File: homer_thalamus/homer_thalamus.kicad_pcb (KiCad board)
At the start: 4 copper layers, 95 x 56 mm, 5 parts, among them J1 GPIO

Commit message: update pcb layout
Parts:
- added A1: RaspberryPi_Pico, Module:RaspberryPi_Pico_Common_Unspecified, F.Cu at (139.2, 72.2)
- added ACC1: GY-521, GY-521:GY-521, F.Cu at (110.3, 61.4)
- added C1: 100n, Capacitor_THT:C_Disc_D4.7mm_W2.5mm_P5.00mm, F.Cu at (178.2, 110.6)
- added D1: LED_RKGB, LED_THT:LED_D5.0mm-4_RGB_Wide_Pins, F.Cu at (174.0, 118.8)
- added J2: MotDrv_Pow_Conn, Connector_JST:JST_XH_B2B-XH-AM_1x02_P2.50mm_Vertical, F.Cu at (77.4, 104.8)
- added J3: Right_Motor_Conn, Connector_PinHeader_2.54mm:PinHeader_1x06_P2.54mm_Vertical, F.Cu at (76.8, 47.0)
- added J4: Left_Motor_Conn, Connector_PinHeader_2.54mm:PinHeader_1x06_P2.54mm_Vertical, F.Cu at (77.6, 97.9)
- added J5: Spare_GP_Conn, Connector_PinHeader_2.54mm:PinHeader_1x10_P2.54mm_Vertical, F.Cu at (140.2, 57.6)
- added J6: VBUS_Conn, Connector_PinHeader_2.54mm:PinHeader_2x02_P2.54mm_Vertical, F.Cu at (177.1, 91.1)
- added R1: 1K, Resistor_THT:R_Axial_DIN0207_L6.3mm_D2.5mm_P7.62mm_Horizontal, F.Cu at (201.6, 90.4)
- added R2: 220R, Resistor_THT:R_Axial_DIN0207_L6.3mm_D2.5mm_P7.62mm_Horizontal, F.Cu at (197.6, 90.4)
- added R3: 220R, Resistor_THT:R_Axial_DIN0207_L6.3mm_D2.5mm_P7.62mm_Horizontal, F.Cu at (193.5, 90.4)
- added R4: 220R, Resistor_THT:R_Axial_DIN0207_L6.3mm_D2.5mm_P7.62mm_Horizontal, F.Cu at (189.5, 90.4)
- added R5: 2K, Resistor_THT:R_Axial_DIN0207_L6.3mm_D2.5mm_P7.62mm_Horizontal, F.Cu at (185.4, 90.4)
- added R6: 1K, Resistor_THT:R_Axial_DIN0207_L6.3mm_D2.5mm_P7.62mm_Horizontal, F.Cu at (181.4, 90.4)
- added SW1: SW_PULLDOWN, Button_Switch_THT:SW_PUSH_6mm, F.Cu at (184.3, 119.2)
- added U1: DRV8874_CARRIER_RIGHT, DRV8874_Carrier:DRV8874_Carrier, F.Cu at (74.6, 65.6)
- added U2: DRV8874_CARRIER_LEFT, DRV8874_Carrier:DRV8874_Carrier, F.Cu at (92.0, 79.8)
- added U3: HC-SR04, HC-SR04:XCVR_HC-SR04, F.Cu at (72.5, 71.9)

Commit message: update pcb layout
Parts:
- moved U2 19.0 mm to (110.8, 76.7)
- moved ACC1 18.9 mm to (91.4, 59.6)
- moved U1 18.1 mm to (92.5, 68.4)
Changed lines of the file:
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@@
 	(footprint "DRV8874_Carrier:DRV8874_Carrier"
 		(layer "F.Cu")
-		(at 74.6373 65.5573 90)
+		(at 92.54 68.44 90)
 		(property "Reference" "U1"
 			(at 13.208 18.796 90)
@@
 			(polygon
 				(pts
-					(xy 74.6427 65.5427) (xy 74.6427 50.3427) (xy 92.4427 50.3427) (xy 92.4427 65.5427)
+					(xy 92.5454 68.4254) (xy 92.5454 53.2254) (xy 110.3454 53.2254) (xy 110.3454 68.4254)
 				)
 			)
@@
 			(polygon
 				(pts
-					(xy 74.6427 65.5427) (xy 74.6427 50.3427) (xy 92.4427 50.3427) (xy 92.4427 65.5427)
+					(xy 92.5454 68.4254) (xy 92.5454 53.2254) (xy 110.3454 53.2254) (xy 110.3454 68.4254)
 				)
 			)
@@
 	(footprint "GY-521:GY-521"
 		(layer "F.Cu")
-		(at 110.2616 61.4334 180)
+		(at 91.4416 59.5934 180)
 		(property "Reference" "ACC1"
 			(at 3.167 -22.8854 0)
@@
 	(footprint "DRV8874_Carrier:DRV8874_Carrier"
 		(layer "F.Cu")
-		(at 92.0027 79.7727 -90)
+		(at 110.78 76.74 -90)
 		(property "Reference" "U2"
 			(at 13.208 18.796 270)
@@
 			(polygon
 				(pts
-					(xy 91.9973 79.7873) (xy 91.9973 94.9873) (xy 74.1973 94.9873) (xy 74.1973 79.7873)
+					(xy 110.7746 76.7546) (xy 110.7746 91.9546) (xy 92.9746 91.9546) (xy 92.9746 76.7546)
 				)
 			)
@@
 			(polygon
 				(pts
-					(xy 91.9973 79.7873) (xy 91.9973 94.9873) (xy 74.1973 94.9873) (xy 74.1973 79.7873)
-				)
-			)
+					(xy 110.7746 76.7546) (xy 110.7746 91.9546) (xy 92.9746 91.9546) (xy 92.9746 76.7546)
+				)
+			)

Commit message: update layout
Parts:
- moved R6 103.9 mm to (78.9, 73.2), turned to 0 degrees
- moved R5 101.0 mm to (86.5, 70.1), turned to 180 degrees
- moved R1 89.4 mm to (112.3, 87.6), turned to 0 degrees
- moved SW1 76.9 mm to (112.7, 91.5), turned to 0 degrees
- moved C1 70.6 mm to (130.3, 58.8), turned to 0 degrees
- moved R2 65.1 mm to (132.8, 96.4), turned to 0 degrees
- moved R3 60.8 mm to (132.8, 93.3), turned to 0 degrees
- moved R4 56.7 mm to (132.8, 90.2), turned to 0 degrees
- moved D1 49.2 mm to (130.2, 96.4), turned to 180 degrees
- moved ACC1 19.7 mm to (111.0, 61.9)
- moved U1 18.1 mm to (74.7, 65.3)
- moved U2 17.1 mm to (94.0, 80.1)
- moved J6 15.2 mm to (162.0, 89.9), turned to 180 degrees
- moved J4 6.31 mm to (83.9, 97.6)
- moved U3 2.53 mm to (75.0, 72.0)
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
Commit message: update pcb layout
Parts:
- added ?: , , F.Cu at (79.3, 80.6)
- added ?: , , F.Cu at (79.3, 63.8)
- moved R5 44.5 mm to (124.1, 94.0)
- moved R6 41.4 mm to (116.4, 90.8)
- moved U1 34.8 mm to (109.2, 69.5), turned to 180 degrees
- moved J2 20.7 mm to (96.6, 97.0), turned to 180 degrees
- moved U2 18.9 mm to (109.2, 91.3), turned to 180 degrees
- moved ACC1 18.0 mm to (93.0, 61.8)
- moved R1 15.1 mm to (124.1, 97.2), turned to 180 degrees
- moved SW1 14.5 mm to (127.2, 92.6)
- moved R2 11.4 mm to (143.6, 92.8), turned to 90 degrees
- moved D1 9.88 mm to (134.0, 87.3)
- moved J4 9.48 mm to (74.5, 97.9)
- moved R3 7.64 mm to (140.4, 92.8), turned to 90 degrees
- moved R4 5.13 mm to (137.2, 92.8), turned to 90 degrees
- moved J6 4.30 mm to (163.1, 85.8), turned to -90 degrees
- moved J5 1.40 mm to (140.3, 56.3)
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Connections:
- J4 pad 5: /ENCA_L -> /ENCB_L
- J4 pad 6: /ENCB_L -> /ENCA_L

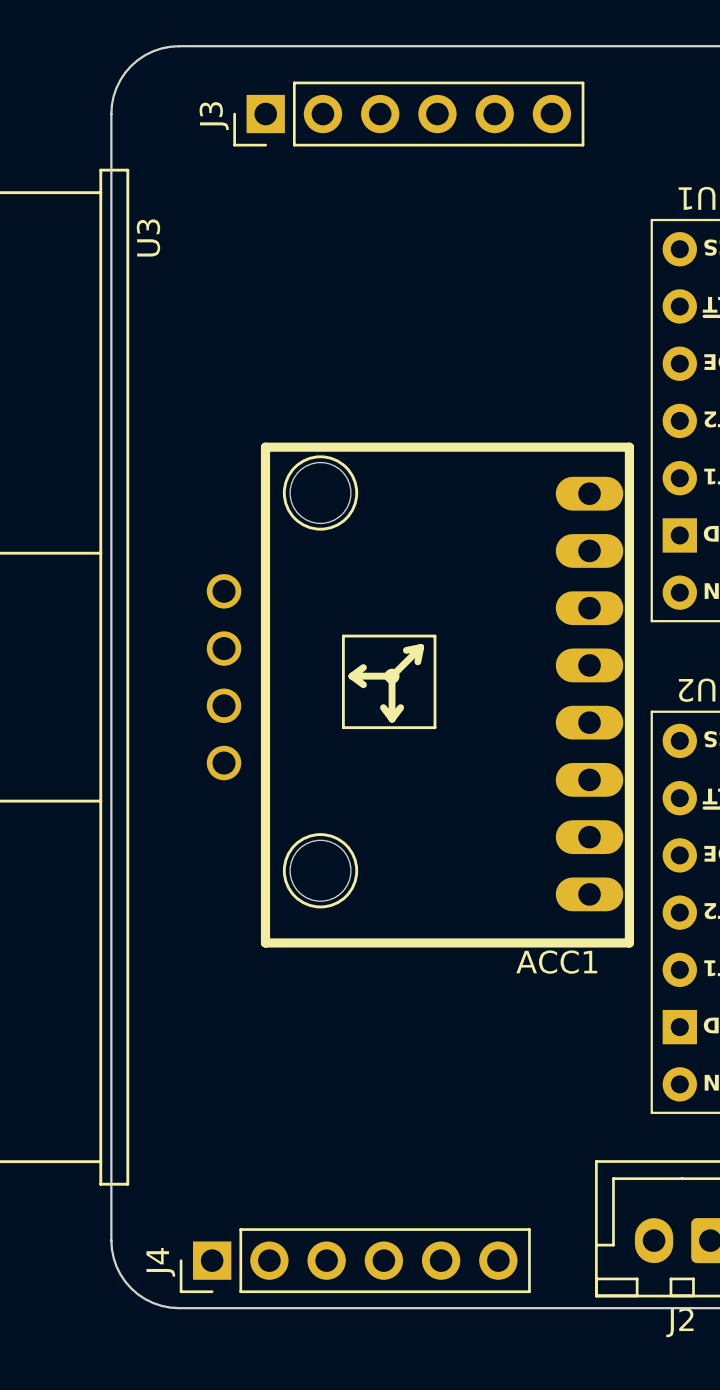
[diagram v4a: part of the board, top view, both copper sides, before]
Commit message: update motor connector position
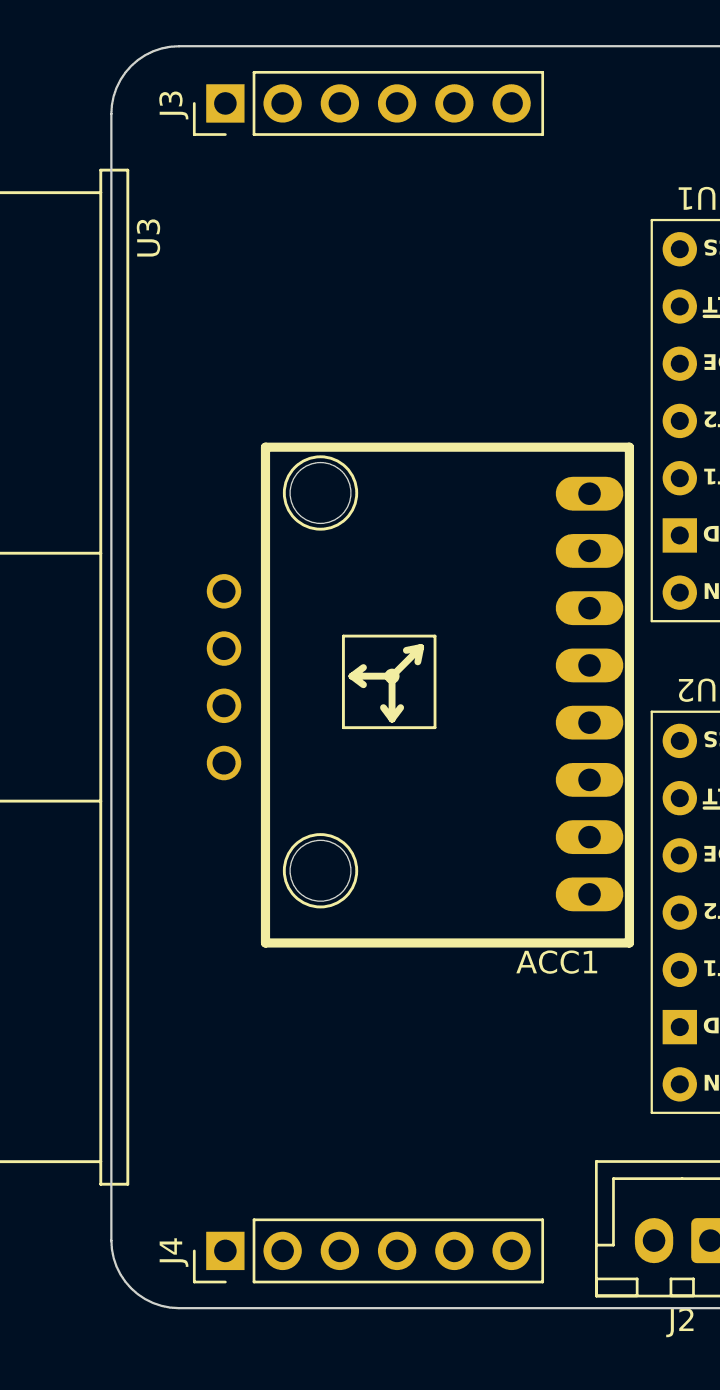
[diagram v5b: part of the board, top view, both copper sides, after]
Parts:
- moved J3 1.85 mm to (75.1, 46.5)
- moved J4 0.73 mm to (75.1, 97.5)
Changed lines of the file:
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@@
 	(footprint "Connector_PinHeader_2.54mm:PinHeader_1x06_P2.54mm_Vertical"
 		(layer "F.Cu")
-		(at 74.473 97.8918 90)
+		(at 75.06 97.46 90)
 		(descr "Through hole straight pin header, 1x06, 2.54mm pitch, single row")
 		(tags "Through hole pin header THT 1x06 2.54mm single row")
@@
 	)
 	(footprint "Connector_PinHeader_2.54mm:PinHeader_1x06_P2.54mm_Vertical"
+		(locked yes)
 		(layer "F.Cu")
-		(at 76.85 47.01 90)
+		(at 75.06 46.54 90)
 		(descr "Through hole straight pin header, 1x06, 2.54mm pitch, single row")
 		(tags "Through hole pin header THT 1x06 2.54mm single row")

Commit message: update pcb layout
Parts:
- moved J5 0.82 mm to (140.3, 55.5)
- moved U1 0.45 mm to (109.6, 69.5)
- moved J2 0.41 mm to (96.2, 96.9)
- moved C1 0.12 mm to (130.1, 58.7)
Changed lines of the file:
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@@
 	(footprint "Connector_JST:JST_XH_B2B-XH-AM_1x02_P2.50mm_Vertical"
 		(layer "F.Cu")
-		(at 96.5818 97.0028 180)
+		(at 96.1754 96.9266 180)
 		(descr "JST XH series connector, B2B-XH-AM, with boss (http://www.jst-mfg.com/product/pdf/eng/eXH.pdf), generated with kicad-footprint-generator")
 		(tags "connector JST XH vertical boss")
 		(property "Reference" "J2"
-			(at 1.25 -3.55 0)
+			(at 6.528 4.032 0)
 			(layer "F.SilkS")
 			(effects
@@
 	(footprint "DRV8874_Carrier:DRV8874_Carrier"
 		(layer "F.Cu")
-		(at 109.1948 69.52 180)
+		(at 109.64 69.46 180)
 		(property "Reference" "U1"
 			(at 13.208 18.796 180)
@@
 			(polygon
 				(pts
-					(xy 109.1802 69.5146) (xy 93.9802 69.5146) (xy 93.9802 51.7146) (xy 109.1802 51.7146)
+					(xy 109.6254 69.4546) (xy 94.4254 69.4546) (xy 94.4254 51.6546) (xy 109.6254 51.6546)
 				)
 			)
@@
 			(polygon
 				(pts
-					(xy 109.1802 69.5146) (xy 93.9802 69.5146) (xy 93.9802 51.7146) (xy 109.1802 51.7146)
+					(xy 109.6254 69.4546) (xy 94.4254 69.4546) (xy 94.4254 51.6546) (xy 109.6254 51.6546)
 				)
 			)
@@
 	(footprint "Capacitor_THT:C_Disc_D4.7mm_W2.5mm_P5.00mm"
 		(layer "F.Cu")
-		(at 130.052 58.598)
+		(at 130.11 58.6996)
 		(descr "C, Disc series, Radial, pin pitch=5.00mm, diameter*width=4.7*2.5mm^2, Capacitor, http://www.vishay.com/docs/45233/krseries.pdf")
 		(tags "C Disc series Radial pin pitch 5.00mm diameter 4.7mm width 2.5mm Capacitor")
@@
 		)
 		(property "Value" "100n"
-			(at 2.5 2.5 0)
-			(layer "F.Fab")
+			(at 2.5108 0.0346 0)
+			(layer "F.SilkS")
 			(effects
 				(font
@@
 	(footprint "Connector_PinHeader_2.54mm:PinHeader_1x10_P2.54mm_Vertical"
 		(layer "F.Cu")
-		(at 140.259 56.312 90)
+		(at 140.27 55.49 90)
 		(descr "Through hole straight pin header, 1x10, 2.54mm pitch, single row")
 		(tags "Through hole pin header THT 1x10 2.54mm single row")
@@
 		)
 	)
-	(group "MDs"
-		(members "6253dd3f-a163-4ecf-acd9-35d704d81902" "75fd1a30-d812-4647-95b3-fe729d1a6444")
-	)
 	(group ""

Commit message: update pcb layout
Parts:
- moved U3 2.46 mm to (72.5, 72.0)
- moved ? 1.75 mm to (77.6, 81.1)
- moved ? 1.75 mm to (77.6, 64.3)
- moved ACC1 1.75 mm to (91.3, 62.3)
- moved U1 1.44 mm to (108.5, 70.4)
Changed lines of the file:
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@@
 		(locked yes)
 		(layer "F.Cu")
-		(at 75 72 -90)
+		(at 72.54 72 -90)
 		(property "Reference" "U3"
-			(at -19.48505 3.31671 90)
+			(at -19.6758 3.0576 90)
 			(layer "F.SilkS")
 			(effects
@@
 		)
 		(property "Value" "HC-SR04"
-			(at 23.8102 3.370695 90)
-			(layer "F.Fab")
+			(at -0.0162 1.6738 90)
+			(layer "F.SilkS")
 			(effects
 				(font
@@
 	(footprint ""
 		(layer "F.Cu")
-		(at 79.2814 80.5906)
+		(at 77.5972 81.077)
 		(property "Reference" ""
 			(at 0 0 0)
@@
 	(footprint "DRV8874_Carrier:DRV8874_Carrier"
 		(layer "F.Cu")
-		(at 109.64 69.46 180)
+		(at 108.52 70.36 180)
 		(property "Reference" "U1"
 			(at 13.208 18.796 180)
@@
 			(polygon
 				(pts
-					(xy 109.6254 69.4546) (xy 94.4254 69.4546) (xy 94.4254 51.6546) (xy 109.6254 51.6546)
+					(xy 108.5054 70.3546) (xy 93.3054 70.3546) (xy 93.3054 52.5546) (xy 108.5054 52.5546)
 				)
 			)
@@
 			(polygon
 				(pts
-					(xy 109.6254 69.4546) (xy 94.4254 69.4546) (xy 94.4254 51.6546) (xy 109.6254 51.6546)
+					(xy 108.5054 70.3546) (xy 93.3054 70.3546) (xy 93.3054 52.5546) (xy 108.5054 52.5546)
 				)
 			)
@@
 	(footprint "GY-521:GY-521"
 		(layer "F.Cu")
-		(at 92.9894 61.7946 180)
+		(at 91.3052 62.281 180)
 		(property "Reference" "ACC1"
 			(at 3.167 -22.8854 0)
@@
 	(footprint ""
 		(layer "F.Cu")
-		(at 79.2814 63.8266)
+		(at 77.5972 64.313)
 		(property "Reference" ""
 			(at 0 0 0)

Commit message: update pcb layout
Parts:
- removed ? (x2): , 
- J2: footprint Connector_JST:JST_XH_B2B-XH-AM_1x02_P2.50mm_Vertical -> Connector_JST:JST_XH_B2B-XH-A_1x02_P2.50mm_Vertical
- moved J2 18.4 mm to (77.8, 96.7)
- moved J4 7.92 mm to (83.0, 97.8)
- moved J3 7.92 mm to (83.0, 46.2)
- moved J5 1.65 mm to (140.3, 53.8)
- moved U1 1.12 mm to (109.6, 70.4)
- moved U2 0.46 mm to (109.6, 91.5)
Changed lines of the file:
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@@
 		(embedded_fonts no)
 	)
-	(footprint "Connector_JST:JST_XH_B2B-XH-AM_1x02_P2.50mm_Vertical"
+	(footprint "Connector_JST:JST_XH_B2B-XH-A_1x02_P2.50mm_Vertical"
 		(layer "F.Cu")
-		(at 96.1754 96.9266 180)
-		(descr "JST XH series connector, B2B-XH-AM, with boss (http://www.jst-mfg.com/product/pdf/eng/eXH.pdf), generated with kicad-footprint-generator")
-		(tags "connector JST XH vertical boss")
+		(at 77.8 96.7 180)
+		(descr "JST XH series connector, B2B-XH-A (http://www.jst-mfg.com/product/pdf/eng/eXH.pdf), generated with kicad-footprint-generator")
+		(tags "connector JST XH vertical")
 		(property "Reference" "J2"
-			(at 6.528 4.032 0)
+			(at -4 3.8 180)
 			(layer "F.SilkS")
 			(effects
@@
 		)
 		(property "Value" "MotDrv_Pow_Conn"
-			(at 1.25 4.6 0)
+			(at 1.25 4.6 180)
 			(layer "F.Fab")
 			(effects
@@
 		)
 		(property "Datasheet" "~"
-			(at 0 0 0)
+			(at 0 0 180)
 			(layer "F.Fab")
 			(hide yes)
@@
 		)
 		(property "Description" "Generic connector, single row, 01x02, script generated (kicad-library-utils/schlib/autogen/connector/)"
-			(at 0 0 0)
+			(at 0 0 180)
 			(layer "F.Fab")
 			(hide yes)
@@
 		)
 		(fp_line
-			(start 1.25 2.75)
-			(end -0.74 2.75)
-			(stroke
-				(width 0.12)
-				(type solid)
-			)
-			(layer "F.SilkS")
-		)
-		(fp_line
 			(start 0.75 -1.7)
 			(end 1.75 -1.7)
@@
 		)
 		(fp_line
+			(start -1.8 2.75)
+			(end 1.25 2.75)
+			(stroke
+				(width 0.12)
+				(type solid)
+			)
+			(layer "F.SilkS")
+		)
+		(fp_line
 			(start -1.8 -0.2)
-			(end -1.8 1.14)
+			(end -1.8 2.75)
 			(stroke
 				(width 0.12)
@@
 		)
 		(fp_text user "${REFERENCE}"
-			(at 1.25 2.7 0)
+			(at 1.25 2.7 180)
 			(layer "F.Fab")
 			(effects
@@
 			)
 		)
-		(pad "" np_thru_hole circle
-			(at -1.6 2 180)
-			(size 1.2 1.2)
-			(drill 1.2)
-			(layers "*.Cu" "*.Mask")
-		)
 		(pad "1" thru_hole roundrect
 			(at 0 0 180)
@@
 		)
 		(embedded_fonts no)
-		(model "${KICAD9_3DMODEL_DIR}/Connector_JST.3dshapes/JST_XH_B2B-XH-AM_1x02_P2.50mm_Vertical.step"
+		(model "${KICAD9_3DMODEL_DIR}/Connector_JST.3dshapes/JST_XH_B2B-XH-A_1x02_P2.50mm_Vertical.step"
 			(offset
 				(xyz 0 0 0)
@@
 		)
 	)
-	(footprint ""
-		(layer "F.Cu")
-		(at 77.5972 81.077)
-		(property "Reference" ""
-			(at 0 0 0)
-			(layer "F.SilkS")
-			(effects
-				(font
-					(size 1.27 1.27)
-					(thickness 0.15)
-				)
-			)
-		)
-		(property "Value" ""
-			(at 0 0 0)
-			(layer "F.Fab")
-			(effects
-				(font
-					(size 1.27 1.27)
-					(thickness 0.15)
-				)
-			)
-		)
-		(property "Datasheet" ""
-			(at 0 0 0)
-			(layer "F.Fab")
-			(hide yes)
-			(effects
-				(font
-					(size 1.27 1.27)
-					(thickness 0.15)
-				)
-			)
-		)
-		(property "Description" ""
-			(at 0 0 0)
-			(layer "F.Fab")
-			(hide yes)
-			(effects
-				(font
-					(size 1.27 1.27)
-					(thickness 0.15)
-				)
-			)
-		)
-		(pad "" np_thru_hole circle
-			(at 0 0)
-			(size 2.7 2.7)
-			(drill 2.7)
-			(layers "*.Cu" "*.Mask")
-		)
-		(embedded_fonts no)
-	)
 	(footprint "Resistor_THT:R_Axial_DIN0207_L6.3mm_D2.5mm_P7.62mm_Horizontal"
 		(layer "F.Cu")
@@
 		)
 		(property "Value" "220R"
-			(at 3.81 2.37 90)
-			(layer "F.Fab")
+			(at 3.901 0.074 90)
+			(layer "F.SilkS")
 			(effects
 				(font
@@
 		)
 		(property "Value" "220R"
-			(at 3.81 2.37 90)
-			(layer "F.Fab")
+			(at 3.821 0.079 90)
+			(layer "F.SilkS")
 			(effects
 				(font
@@
 	)
 	(footprint "DRV8874_Carrier:DRV8874_Carrier"
+		(locked yes)
 		(layer "F.Cu")
-		(at 108.52 70.36 180)
+		(at 109.64 70.351 180)
 		(property "Reference" "U1"
 			(at 13.208 18.796 180)
@@
 			(polygon
 				(pts
-					(xy 108.5054 70.3546) (xy 93.3054 70.3546) (xy 93.3054 52.5546) (xy 108.5054 52.5546)
+					(xy 109.6254 70.3456) (xy 94.4254 70.3456) (xy 94.4254 52.5456) (xy 109.6254 52.5456)
 				)
 			)
@@
 			(polygon
 				(pts
-					(xy 108.5054 70.3546) (xy 93.3054 70.3546) (xy 93.3054 52.5546) (xy 108.5054 52.5546)
+					(xy 109.6254 70.3456) (xy 94.4254 70.3456) (xy 94.4254 52.5456) (xy 109.6254 52.5456)
 				)
 			)
@@
 		)
 		(property "Value" "220R"
-			(at 3.81 2.37 90)
-			(layer "F.Fab")
+			(at 3.821 -0.031 90)
+			(layer "F.SilkS")
 			(effects
 				(font
@@
 	)
 	(footprint "DRV8874_Carrier:DRV8874_Carrier"
+		(locked yes)
 		(layer "F.Cu")
-		(at 109.1948 91.3386 180)
+		(at 109.64 91.454 180)
 		(property "Reference" "U2"
 			(at 13.208 18.796 180)
@@
 			(polygon
 				(pts
-					(xy 109.1802 91.3332) (xy 93.9802 91.3332) (xy 93.9802 73.5332) (xy 109.1802 73.5332)
+					(xy 109.6254 91.4486) (xy 94.4254 91.4486) (xy 94.4254 73.6486) (xy 109.6254 73.6486)
 				)
 			)
@@
 			(polygon
 				(pts
-					(xy 109.1802 91.3332) (xy 93.9802 91.3332) (xy 93.9802 73.5332) (xy 109.1802 73.5332)
+					(xy 109.6254 91.4486) (xy 94.4254 91.4486) (xy 94.4254 73.6486) (xy 109.6254 73.6486)
 				)
 			)
@@
 	(footprint "Connector_PinHeader_2.54mm:PinHeader_2x02_P2.54mm_Vertical"
 		(layer "F.Cu")
-		(at 163.119 85.776 -90)
+		(at 163.13 85.776 -90)
 		(descr "Through hole straight pin header, 2x02, 2.54mm pitch, double rows")
 		(tags "Through hole pin header THT 2x02 2.54mm double row")
@@
 	)
 	(footprint "Connector_PinHeader_2.54mm:PinHeader_1x06_P2.54mm_Vertical"
+		(locked yes)
 		(layer "F.Cu")
-		(at 75.06 97.46 90)
+		(at 82.97 97.804 90)
 		(descr "Through hole straight pin header, 1x06, 2.54mm pitch, single row")
 		(tags "Through hole pin header THT 1x06 2.54mm single row")
 		(property "Reference" "J4"
-			(at 0 -2.38 90)
+			(at 2.772 15.03 180)
 			(layer "F.SilkS")
 			(effects
@@
 		)
 	)
-	(footprint ""
-		(layer "F.Cu")
-		(at 77.5972 64.313)
-		(property "Reference" ""
-			(at 0 0 0)
-			(layer "F.SilkS")
-			(effects
-				(font
-					(size 1.27 1.27)
-					(thickness 0.15)
-				)
-			)
-		)
-		(property "Value" ""
-			(at 0 0 0)
-			(layer "F.Fab")
-			(effects
-				(font
-					(size 1.27 1.27)
-					(thickness 0.15)
-				)
-			)
-		)
-		(property "Datasheet" ""
-			(at 0 0 0)
-			(layer "F.Fab")
-			(hide yes)
-			(effects
-				(font
-					(size 1.27 1.27)
-					(thickness 0.15)
-				)
-			)
-		)
-		(property "Description" ""
-			(at 0 0 0)
-			(layer "F.Fab")
-			(hide yes)
-			(effects
-				(font
-					(size 1.27 1.27)
-					(thickness 0.15)
-				)
-			)
-		)
-		(pad "" np_thru_hole circle
-			(at 0 0)
-			(size 2.7 2.7)
-			(drill 2.7)
-			(layers "*.Cu" "*.Mask")
-		)
-		(embedded_fonts no)
-	)
 	(footprint "MountingHole:MountingHole_2.7mm_M2.5"
 		(locked yes)
@@
 		(locked yes)
 		(layer "F.Cu")
-		(at 75.06 46.54 90)
+		(at 82.97 46.221 90)
 		(descr "Through hole straight pin header, 1x06, 2.54mm pitch, single row")
 		(tags "Through hole pin header THT 1x06 2.54mm single row")
@@
 	(footprint "Connector_PinHeader_2.54mm:PinHeader_1x10_P2.54mm_Vertical"
 		(layer "F.Cu")
-		(at 140.27 55.49 90)
+		(at 140.27 53.841 90)
 		(descr "Through hole straight pin header, 1x10, 2.54mm pitch, single row")
 		(tags "Through hole pin header THT 1x10 2.54mm single row")
@@
 	)
 	(footprint "Connector_PinSocket_2.54mm:PinSocket_2x20_P2.54mm_Vertical"
+		(locked yes)
 		(layer "B.Cu")
 		(at 108.37 48.77 -90)
@@
 		)
 	)
-	(group ""
-		(members "35ee8997-3f2a-4b5e-803e-bd100146d691" "6c9ee477-ee9e-4c52-810e-ce4e0f08e68e"
-			"c026d8c6-f0da-4360-92ad-d7038d78206f"
-		)
-	)
-	(group ""
-		(members "486ff44f-b3ec-4e19-88da-b600e7583e51" "5e6b1514-5a17-4e1c-8447-1c20f33800fc"
-			"67a43284-ba4a-466a-9054-f3dc82ac6bba"
-		)
-	)
